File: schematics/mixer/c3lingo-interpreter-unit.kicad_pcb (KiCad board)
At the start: 2 copper layers, 162 x 87 mm, 89 parts, among them J1 Headphone 1, J2 Mic 1, J3 Mix Line-Out, J4 Stage Line-In, J5 PowerSupply, J6 PowerSupply, J7 PowerSupply, SW1 Mute_1, SW2 OnAir_1, U1 LM833N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

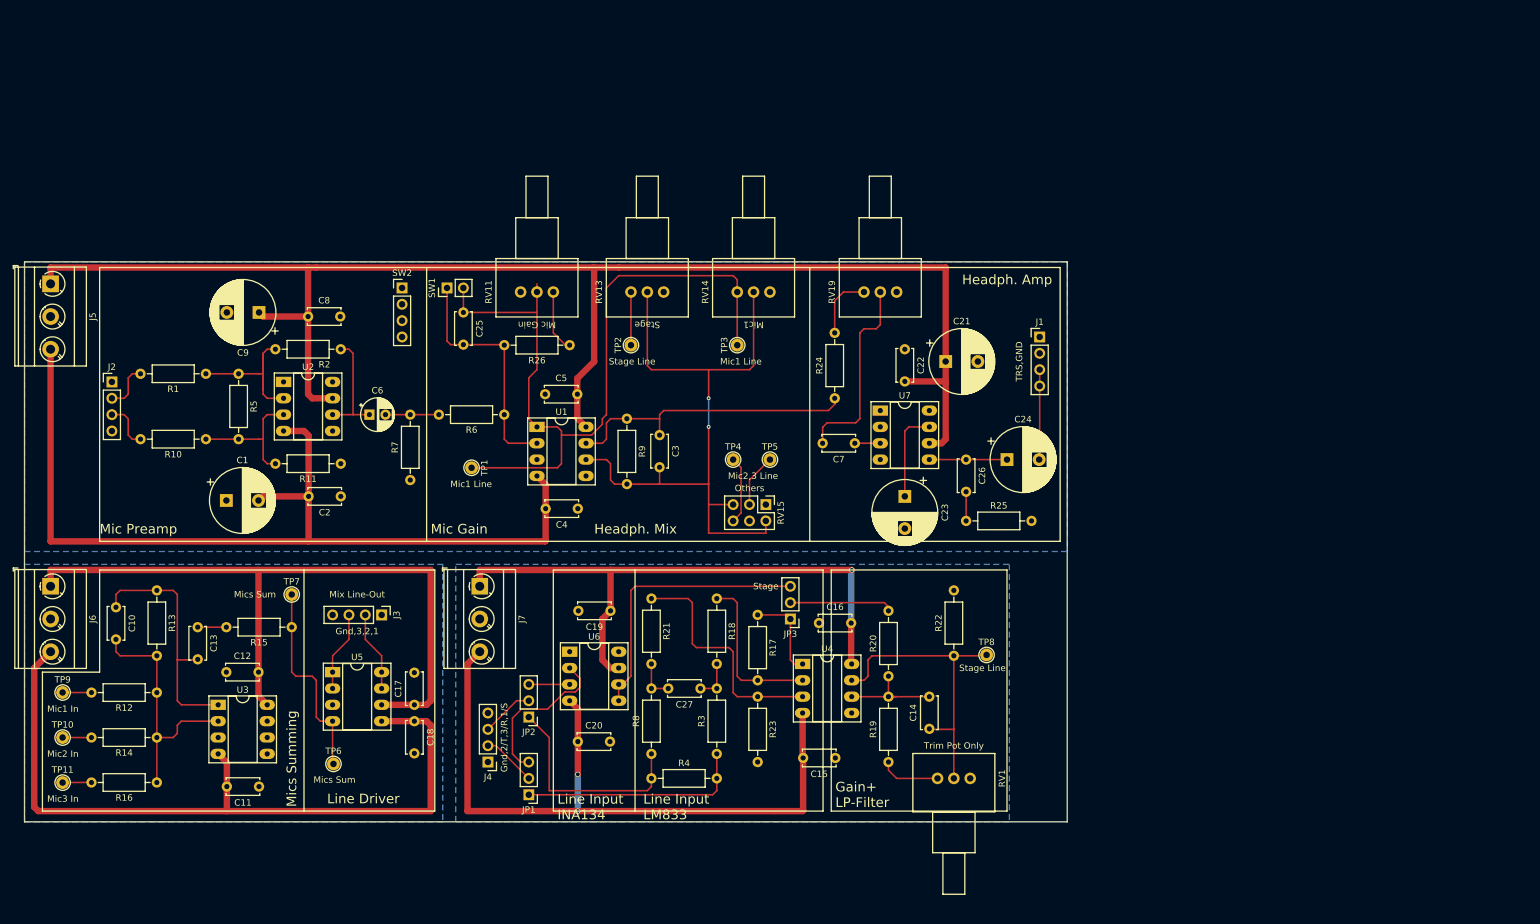
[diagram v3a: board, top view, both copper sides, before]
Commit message: Main: Summing design flaw fixed; better headphone vol. range
- Multiple R and C value adaptions
- Line Input: No relevant difference between INA134 and own circuit -> LM833 chosen
- Signal busses/ summing module inputs fixed
- TODO: On-Air Button
- TODO: Update PCB layout
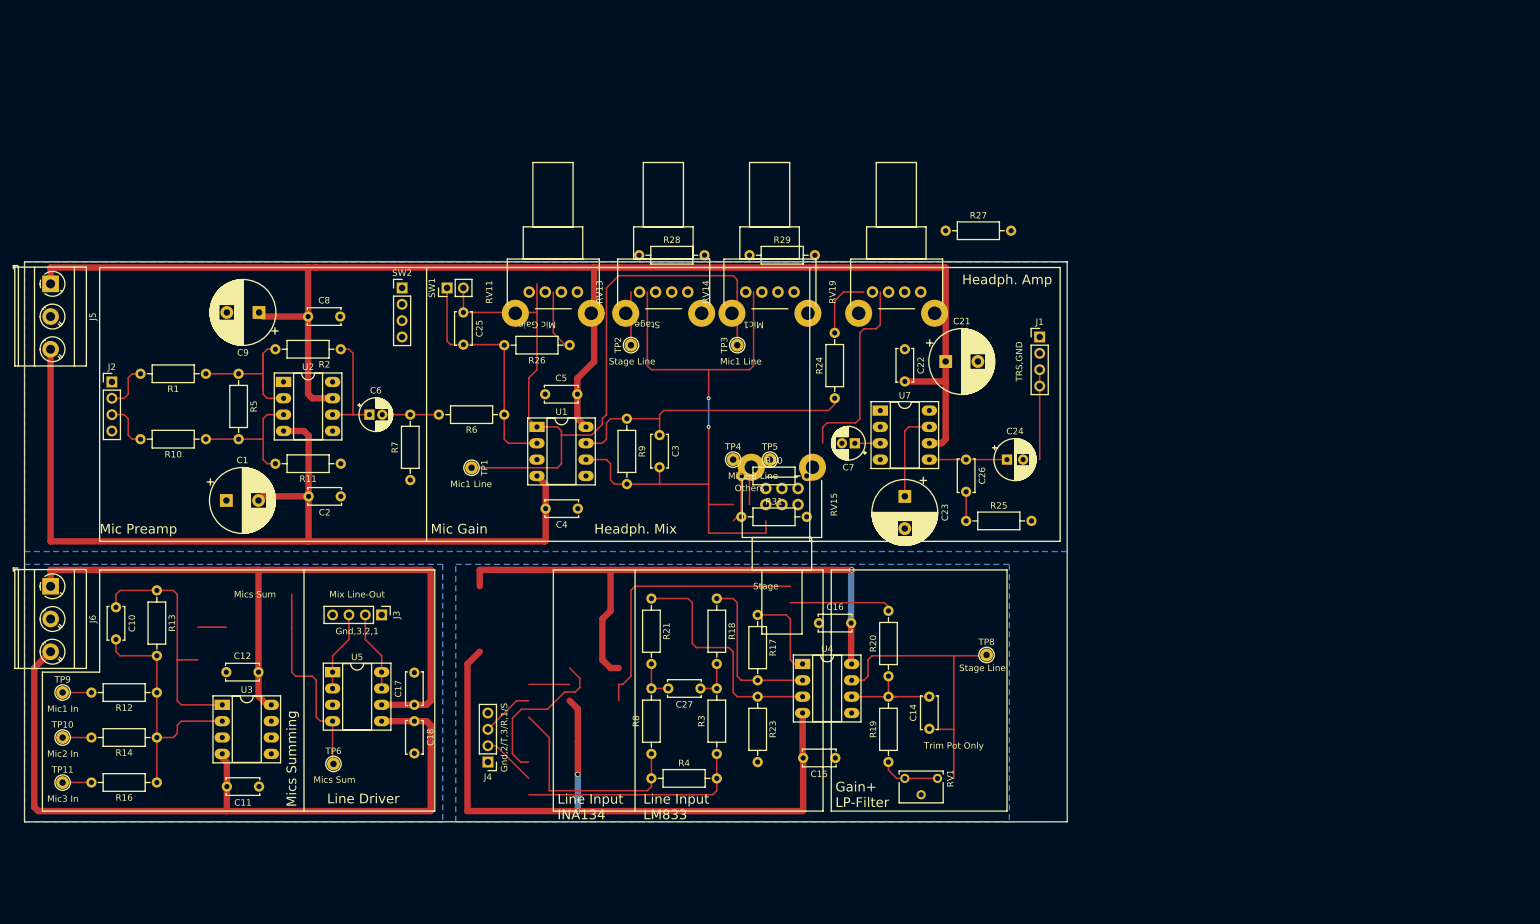
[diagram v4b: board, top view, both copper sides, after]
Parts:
- removed C13: 4.7pF, Capacitor_THT:C_Disc_D5.0mm_W2.5mm_P5.00mm
- removed C19, C20: 1uF, Capacitor_THT:C_Disc_D5.0mm_W2.5mm_P5.00mm
- removed J7: PowerSupply, TerminalBlock_MetzConnect:TerminalBlock_MetzConnect_Type073_RT02603HBLU_1x03_P5.08mm_Horizontal
- removed JP1: Stage Hot, Connector_PinHeader_2.54mm:PinHeader_1x03_P2.54mm_Vertical
- removed JP2: Stage Cold, Connector_PinHeader_2.54mm:PinHeader_1x03_P2.54mm_Vertical
- removed JP3: Stage Out, Connector_PinHeader_2.54mm:PinHeader_1x03_P2.54mm_Vertical
- removed R15: 47R, Resistor_THT:R_Axial_DIN0207_L6.3mm_D2.5mm_P10.16mm_Horizontal
- removed R22: 22K, Resistor_THT:R_Axial_DIN0207_L6.3mm_D2.5mm_P10.16mm_Horizontal
- removed TP7: MicSum, TestPoint:TestPoint_THTPad_D2.0mm_Drill1.0mm
- removed U6: INA134PA, Package_DIP:DIP-8_W7.62mm_Socket_LongPads
- added R27: 2.2K, Resistor_THT:R_Axial_DIN0207_L6.3mm_D2.5mm_P10.16mm_Horizontal, F.Cu at (158.1, 10.2)
- added R28: 22K, Resistor_THT:R_Axial_DIN0207_L6.3mm_D2.5mm_P10.16mm_Horizontal, F.Cu at (110.5, 14.0)
- added R29: 22K, Resistor_THT:R_Axial_DIN0207_L6.3mm_D2.5mm_P10.16mm_Horizontal, F.Cu at (127.6, 14.0)
- added R30: 22K, Resistor_THT:R_Axial_DIN0207_L6.3mm_D2.5mm_P10.16mm_Horizontal, F.Cu at (126.4, 48.3)
- added R31: 22K, Resistor_THT:R_Axial_DIN0207_L6.3mm_D2.5mm_P10.16mm_Horizontal, F.Cu at (126.4, 54.6)
- C24: footprint Capacitor_THT:CP_Radial_D10.0mm_P5.00mm -> Capacitor_THT:CP_Radial_D6.3mm_P2.50mm
- C25: value 0.1uF -> 100nF
- C27: value 220p -> 220pF
- C6: value 10uF -> 1uF; footprint Capacitor_THT:CP_Radial_D5.0mm_P2.50mm -> Capacitor_THT:CP_Radial_D5.0mm_P2.00mm
- C7: value 100nF -> 1uF; footprint Capacitor_THT:C_Disc_D5.0mm_W2.5mm_P5.00mm -> Capacitor_THT:CP_Radial_D5.0mm_P2.00mm
- R24: value 820K -> 330K
- R26: value 220R -> 270R
- R6: value 820R -> 1.5K
- R7: value 5.6K -> 470R
- RV1: footprint Potentiometer_THT:Potentiometer_Vishay_148-149_Single_Horizontal -> Potentiometer_THT:Potentiometer_Vishay_T73XX_Horizontal
- RV11, RV19: value 25K -> 50K log.; footprint Potentiometer_THT:Potentiometer_Vishay_148-149_Single_Horizontal -> JBeyerstedt-Library:Potentiometer_Alps_RK11K_Single_Horizontal
- RV13, RV14: value 22K -> 50K log.; footprint Potentiometer_THT:Potentiometer_Vishay_148-149_Single_Horizontal -> JBeyerstedt-Library:Potentiometer_Alps_RK11K_Single_Horizontal
- RV15: value 22K -> 50K log. st.; footprint Connector_PinHeader_2.54mm:PinHeader_2x03_P2.54mm_Vertical -> Potentiometer_THT:Potentiometer_Alps_RK09L_Double_Horizontal
- moved U3 0.63 mm to (45.7, 83.8)
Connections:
- R17 pad 1: Net-(JP3-Pad1) -> Net-(R17-Pad1)
- R20 pad 2: Net-(JP3-Pad2) -> Net-(R17-Pad1)
- R3 pad 1: Net-(JP1-Pad1) -> Net-(J4-Pad2)
- R4 pad 1: Net-(JP2-Pad1) -> Net-(J4-Pad3)
- R4 pad 2: Net-(JP1-Pad1) -> Net-(J4-Pad2)
- R8 pad 1: Net-(JP2-Pad1) -> Net-(J4-Pad3)
- RV13 pad 2: Net-(C3-Pad2) -> Net-(R28-Pad2)
- RV14 pad 2: Net-(C3-Pad2) -> Net-(R29-Pad2)
- RV15 pad 2: Net-(C3-Pad2) -> Net-(R31-Pad2)
- RV15 pad 5: Net-(C3-Pad2) -> Net-(R30-Pad2)
- RV19 pad 1: GNDREF -> Net-(R27-Pad1)
- RV19 pad 2: Net-(C7-Pad2) -> Net-(C7-Pad1)
- TP6 pad 1: MicSum -> Net-(C10-Pad1)
- U4 pad 1: Net-(JP3-Pad1) -> Net-(R17-Pad1)
- U5 pad 4: MicSum -> Net-(C10-Pad1)
- U7 pad 3: Net-(C7-Pad1) -> Net-(C7-Pad2)
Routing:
- net Net-(JP1-Pad1): track 35.2 -> 0.00 mm
- net Net-(J4-Pad2): track 8.45 -> 43.6 mm
- net Net-(JP2-Pad1): track 34.0 -> 0.00 mm
- net Net-(J4-Pad3): track 8.19 -> 42.2 mm
- net MicSum: track 31.6 -> 0.00 mm
- net Net-(C10-Pad1): track 38.4 -> 70.0 mm
- net Net-(R17-Pad1): track 0.00 -> 30.0 mm
- net Net-(JP3-Pad2): track 16.1 -> 0.00 mm
- net Net-(JP3-Pad1): track 13.9 -> 0.00 mm

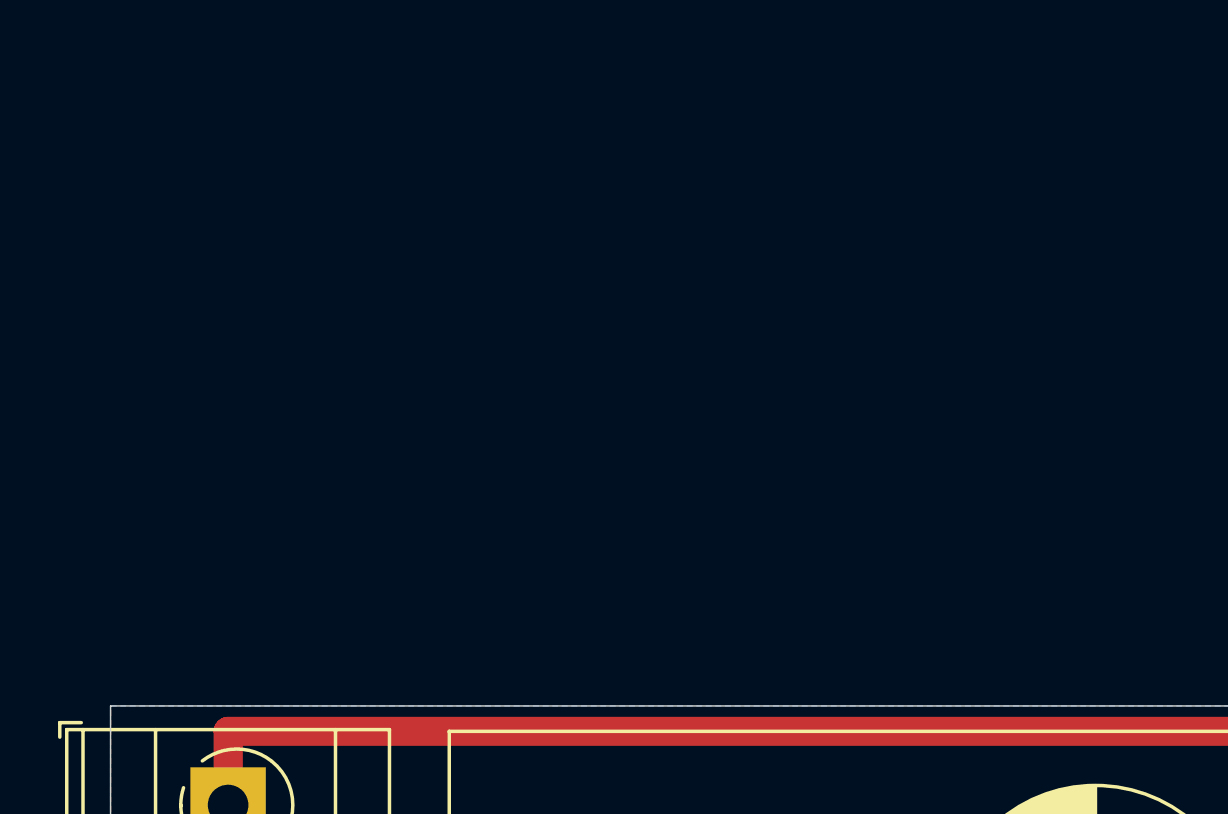
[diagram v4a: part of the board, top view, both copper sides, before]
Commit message: Main: Add 15V phantom power
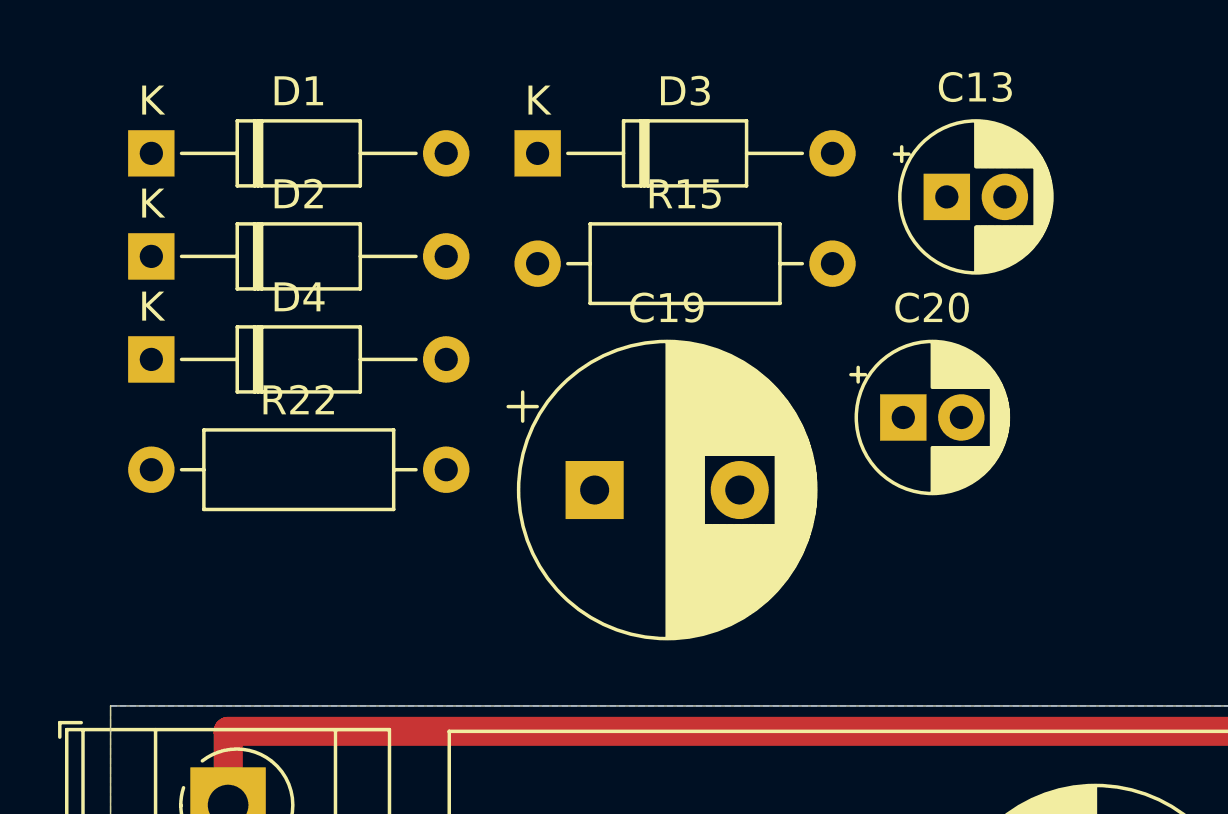
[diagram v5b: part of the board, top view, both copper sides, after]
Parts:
- added C13: 1uF, Capacitor_THT:CP_Radial_D5.0mm_P2.00mm, F.Cu at (43.8, -2.54)
- added C19: 100uF, Capacitor_THT:CP_Radial_D10.0mm_P5.00mm, F.Cu at (31.7, 7.56)
- added C20: 1uF, Capacitor_THT:CP_Radial_D5.0mm_P2.00mm, F.Cu at (42.3, 5.06)
- added D1: 1N4148, Diode_THT:D_DO-35_SOD27_P10.16mm_Horizontal, F.Cu at (16.4, -4.04)
- added D2: 1N4148, Diode_THT:D_DO-35_SOD27_P10.16mm_Horizontal, F.Cu at (16.4, -0.49)
- added D3: 1N4148, Diode_THT:D_DO-35_SOD27_P10.16mm_Horizontal, F.Cu at (29.7, -4.04)
- added D4: 1N4148, Diode_THT:D_DO-35_SOD27_P10.16mm_Horizontal, F.Cu at (16.4, 3.06)
- added R15: 680R 1%, Resistor_THT:R_Axial_DIN0207_L6.3mm_D2.5mm_P10.16mm_Horizontal, F.Cu at (29.7, -0.24)
- added R22: 680R 1%, Resistor_THT:R_Axial_DIN0207_L6.3mm_D2.5mm_P10.16mm_Horizontal, F.Cu at (16.4, 6.86)
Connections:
- net GNDREF renamed GND
- J2 pad 2: Net-(J2-Pad2) -> Net-(C13-Pad1)
- J2 pad 3: Net-(J2-Pad3) -> Net-(C20-Pad1)
- R1 pad 2: Net-(J2-Pad2) -> Net-(C13-Pad2)
- R10 pad 2: Net-(J2-Pad3) -> Net-(C20-Pad2)
